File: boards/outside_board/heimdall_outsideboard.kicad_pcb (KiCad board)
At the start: 2 copper layers, 6 parts, among them J1 Conn_01x09, J2 Conn_01x06

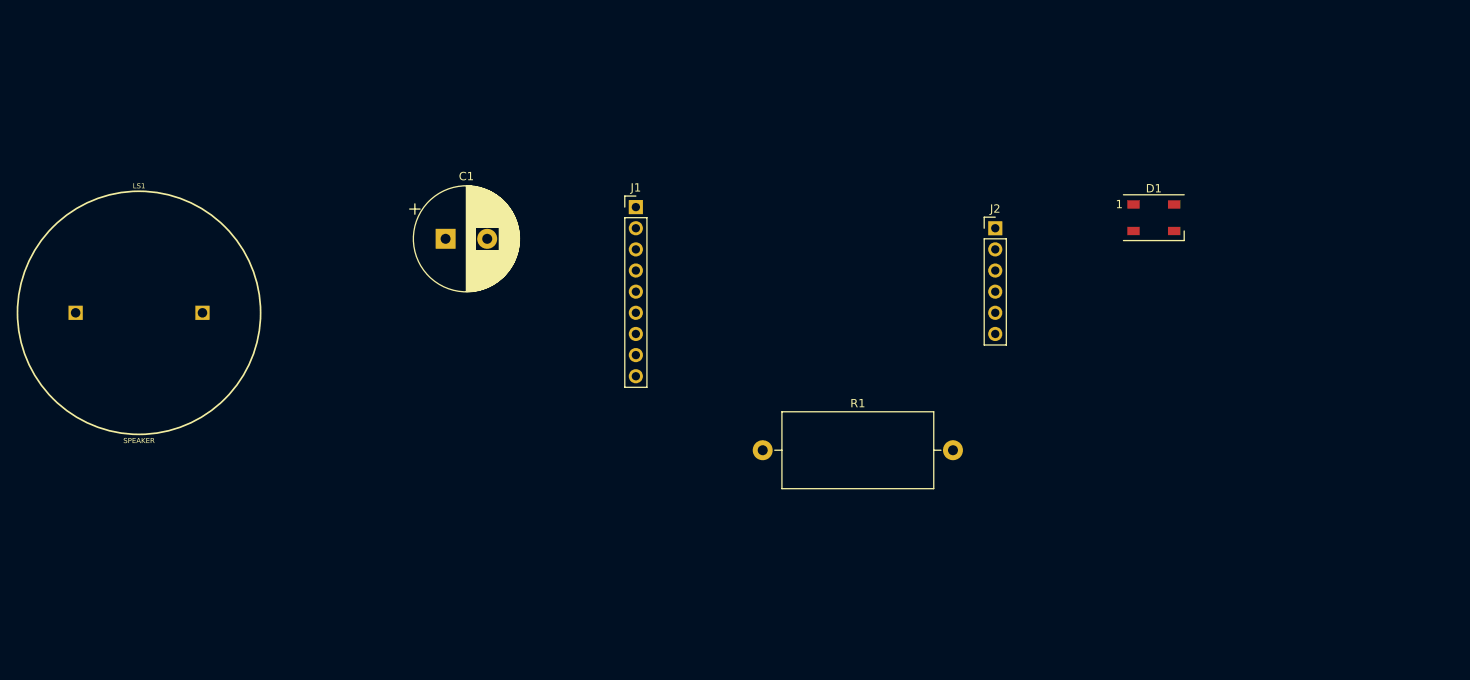
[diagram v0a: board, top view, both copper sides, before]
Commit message: Outside board design: more PCB layout
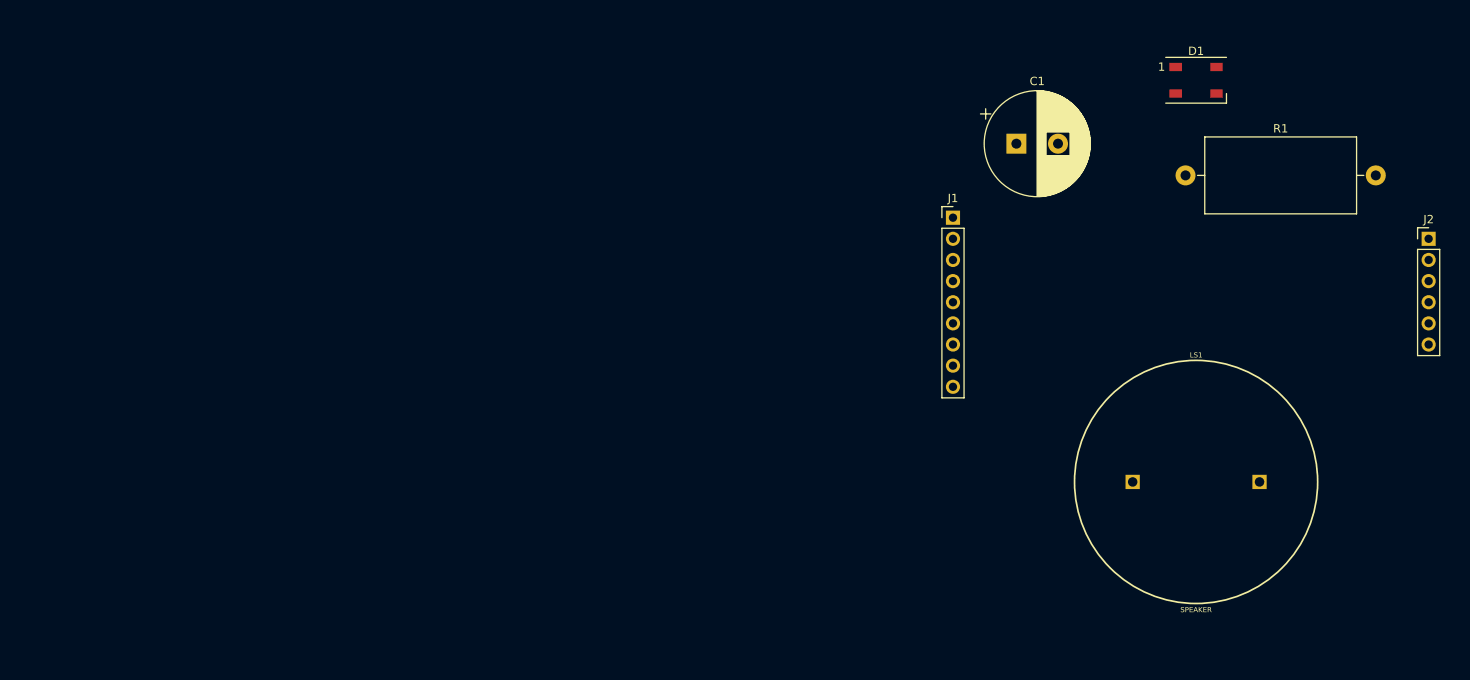
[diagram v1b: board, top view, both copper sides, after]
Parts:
- moved LS1 128.6 mm to (83.8, 130.8)
- moved C1 69.5 mm to (62.2, 90.2)
- moved R1 60.6 mm to (82.5, 94.0)
- moved J2 52.1 mm to (111.8, 101.6)
- moved J1 38.1 mm to (54.6, 99.1)
- moved D1 17.3 mm to (83.8, 82.5)

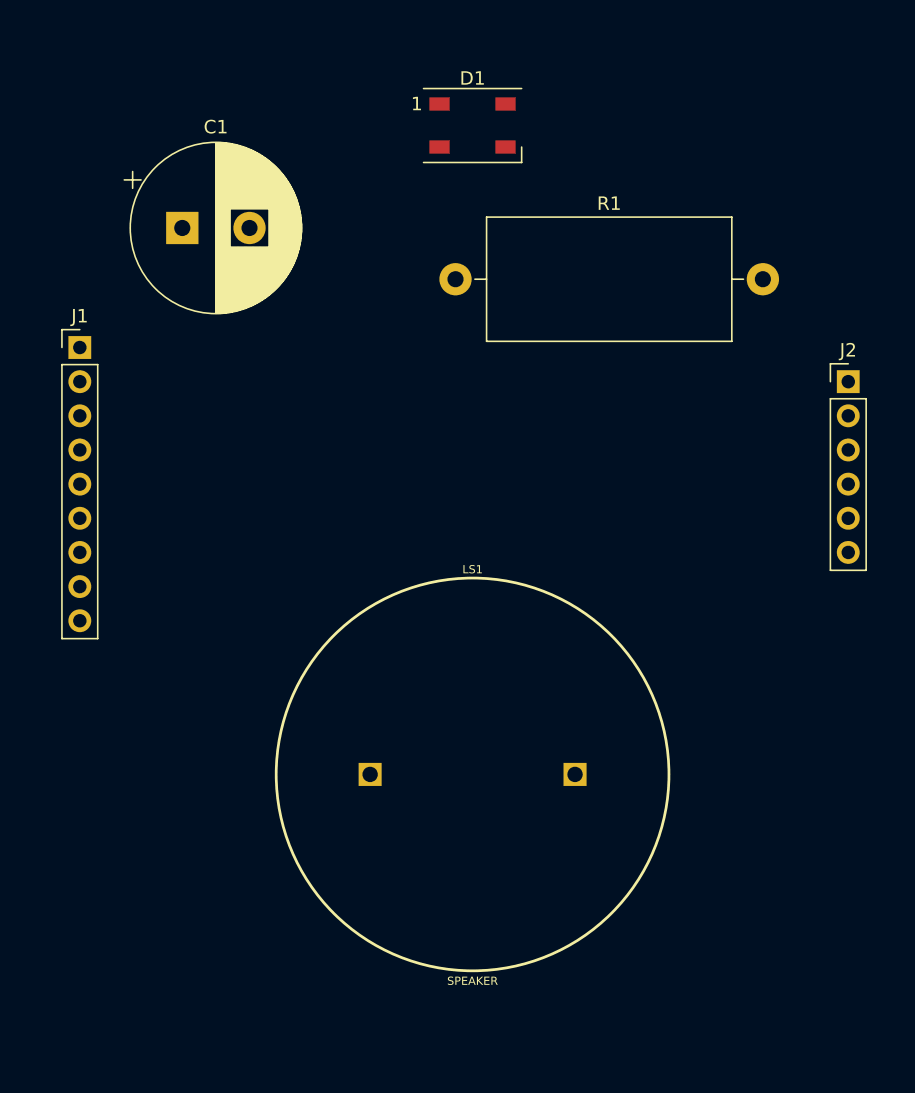
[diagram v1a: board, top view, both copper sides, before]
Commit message: Outside board: replace the pin headers with screw terminals
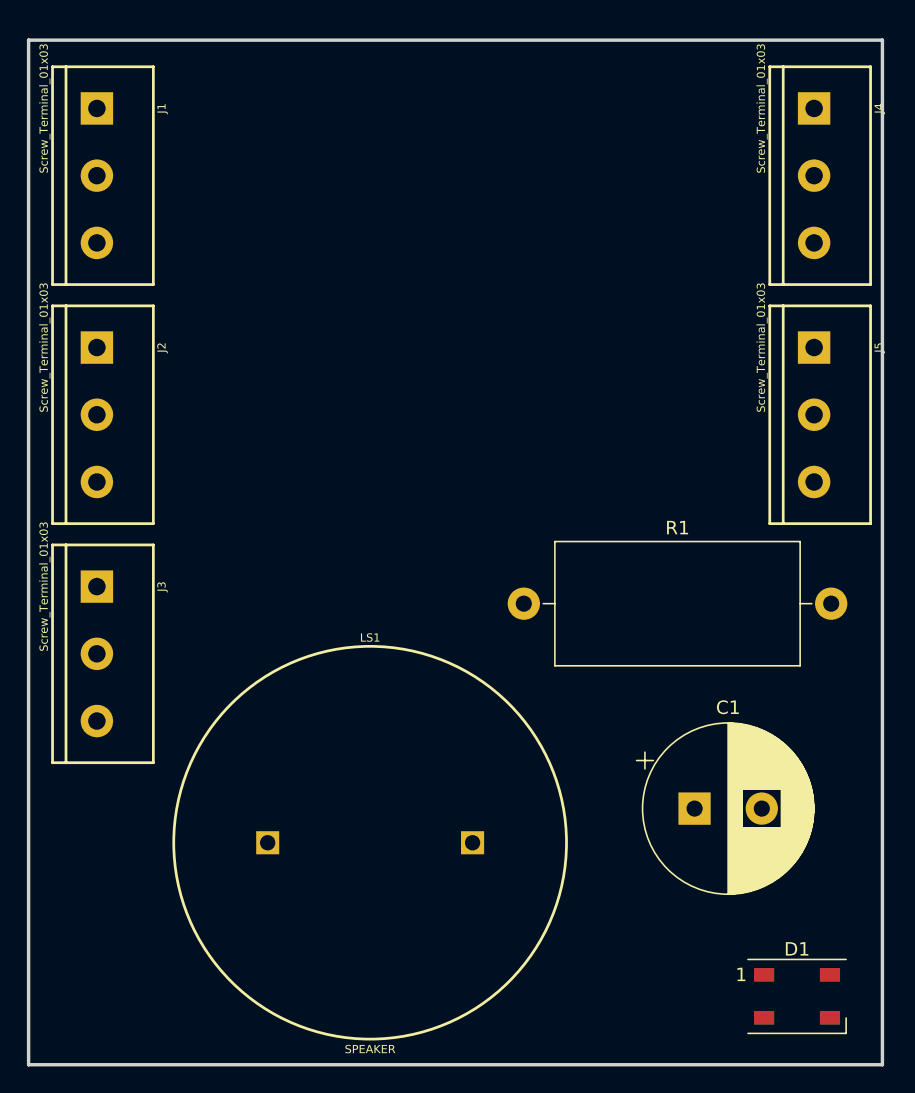
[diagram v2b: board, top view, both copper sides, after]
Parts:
- added J3: Screw_Terminal_01x03, Connectors:SCREWTERMINAL-5MM-3, F.Cu at (55.9, 116.8)
- added J4: Screw_Terminal_01x03, Connectors:SCREWTERMINAL-5MM-3, F.Cu at (109.2, 81.3)
- added J5: Screw_Terminal_01x03, Connectors:SCREWTERMINAL-5MM-3, F.Cu at (109.2, 99.1)
- J1: value Conn_01x09 -> Screw_Terminal_01x03; footprint Connector_PinHeader_2.54mm:PinHeader_1x09_P2.54mm_Vertical -> Connectors:SCREWTERMINAL-5MM-3
- J2: value Conn_01x06 -> Screw_Terminal_01x03; footprint Connector_PinHeader_2.54mm:PinHeader_1x06_P2.54mm_Vertical -> Connectors:SCREWTERMINAL-5MM-3
- moved D1 69.1 mm to (108.0, 147.3)
- moved C1 57.6 mm to (100.3, 133.3)
- moved J2 55.9 mm to (55.9, 99.1), turned to 270 degrees
- moved R1 24.7 mm to (87.6, 118.1)
- moved J1 17.8 mm to (55.9, 81.3), turned to 270 degrees
- moved LS1 9.16 mm to (76.2, 135.9)
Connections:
- J2 pad 1: /+3V3 -> /CS
- J2 pad 2: /GND -> /SCK
- J2 pad 3: /CS -> /MOSI
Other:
- board outline added: 63.5 x 76.2 mm

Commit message: Revert "Outside board: replace the pin headers with screw terminals"
This reverts commit 695c30ad44e01b6420bbd27eb88eba567c36bb63.
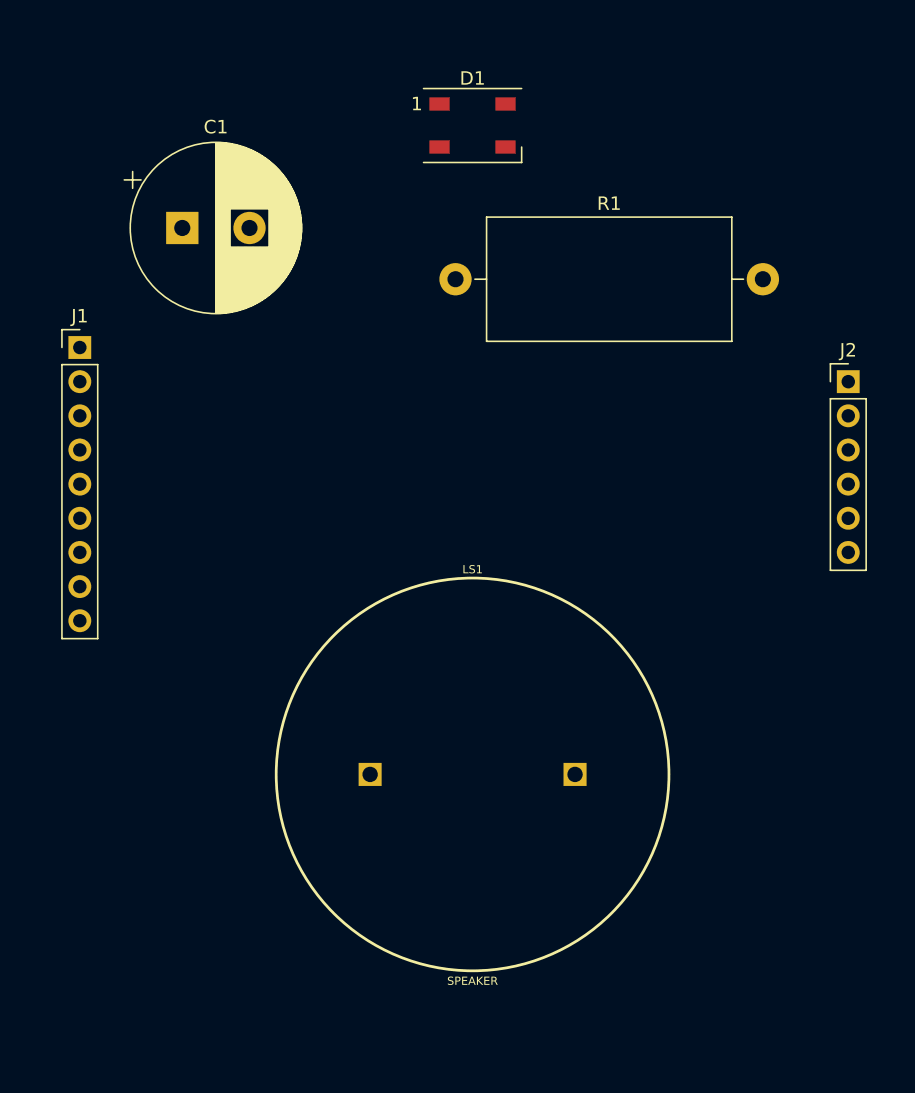
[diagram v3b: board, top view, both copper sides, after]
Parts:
- removed J3, J4, J5: Screw_Terminal_01x03, Connectors:SCREWTERMINAL-5MM-3
- J1: value Screw_Terminal_01x03 -> Conn_01x09; footprint Connectors:SCREWTERMINAL-5MM-3 -> Connector_PinHeader_2.54mm:PinHeader_1x09_P2.54mm_Vertical
- J2: value Screw_Terminal_01x03 -> Conn_01x06; footprint Connectors:SCREWTERMINAL-5MM-3 -> Connector_PinHeader_2.54mm:PinHeader_1x06_P2.54mm_Vertical
- moved D1 69.1 mm to (83.8, 82.5)
- moved C1 57.6 mm to (62.2, 90.2)
- moved J2 55.9 mm to (111.8, 101.6), turned to 0 degrees
- moved R1 24.7 mm to (82.5, 94.0)
- moved J1 17.8 mm to (54.6, 99.1), turned to 0 degrees
- moved LS1 9.16 mm to (83.8, 130.8)
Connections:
- J2 pad 1: /CS -> /+3V3
- J2 pad 2: /SCK -> /GND
- J2 pad 3: /MOSI -> /CS
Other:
- board outline removed

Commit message: More outside board PCB layout.
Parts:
- moved R1 29.8 mm to (59.7, 113.0)
- moved LS1 17.3 mm to (67.3, 135.9)
- moved J2 15.9 mm to (97.8, 94.0)
- moved D1 9.15 mm to (93.0, 82.8)
- moved J1 7.62 mm to (54.6, 91.4)
- moved C1 7.18 mm to (67.3, 85.1)
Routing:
- net Net-(D1-Pad4): track 0.00 -> 51.8 mm
- net /SCK: track 0.00 -> 43.2 mm
- net /MOSI: track 0.00 -> 43.2 mm
- net /MISO: track 0.00 -> 43.2 mm
- net /GND: track 0.00 -> 43.2 mm
- net /CS: track 0.00 -> 43.2 mm
- net /+3V3: track 0.00 -> 43.2 mm
- net /+5V: track 0.00 -> 41.2 mm
- net /Buzzer: track 0.00 -> 27.9 mm
- net /LED: track 0.00 -> 8.00 mm
- added copper zone on B.Cu, net /GND
- added copper zone on F.Cu, net /GND
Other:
- board outline added: 50.8 x 76.2 mm
- board text added: "Heimdall Access Control Board"
- board text added: "github.com/makesaltlake/heimdall"

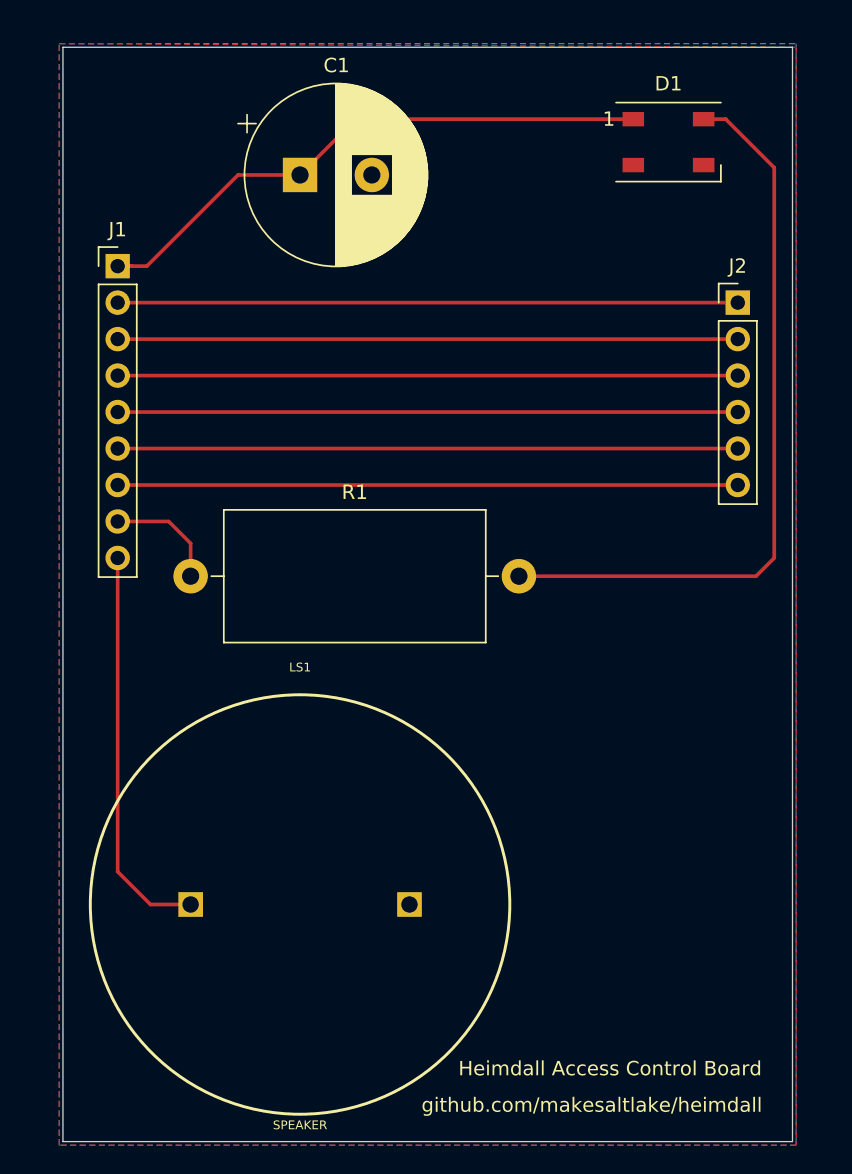
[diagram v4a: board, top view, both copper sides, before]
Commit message: Update outside board schematics and board layout
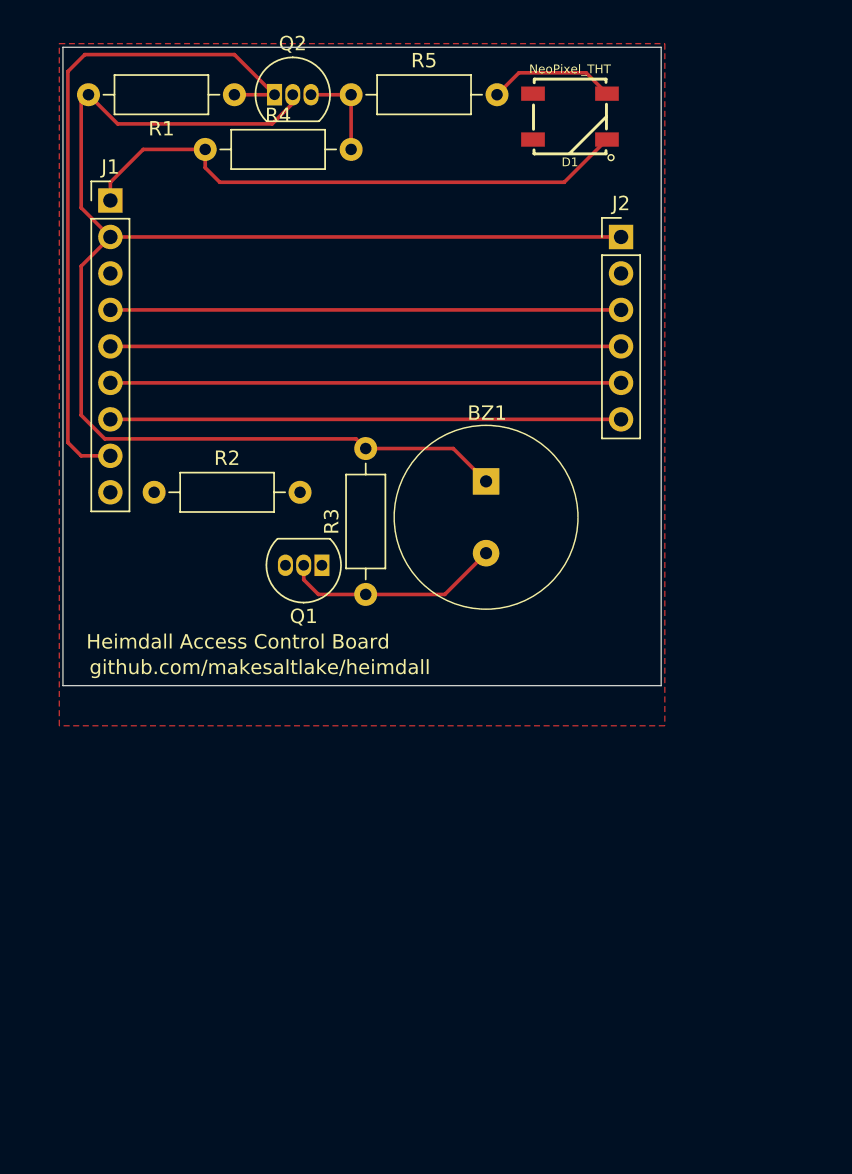
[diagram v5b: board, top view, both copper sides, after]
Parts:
- removed C1: 1000UF-RADIAL-5MM-25V-20%, Capacitor_THT:CP_Radial_D12.5mm_P5.00mm
- removed LS1: SPEAKER, Electromechanical:PCB_MOUNT_SPEAKER
- added BZ1: PS1240P02BT, digikey-footprints:Piezo_Transducer_THT_PS1240P02BT, F.Cu at (80.3, 106.4)
- added Q1: 2N3904, Package_TO_SOT_THT:TO-92_Inline, F.Cu at (68.8, 112.3)
- added Q2: 2N7000, Package_TO_SOT_THT:TO-92_Inline, F.Cu at (65.5, 79.5)
- added R2: 1K, Resistor_THT:R_Axial_DIN0207_L6.3mm_D2.5mm_P10.16mm_Horizontal, F.Cu at (57.1, 107.2)
- added R3: 1K, Resistor_THT:R_Axial_DIN0207_L6.3mm_D2.5mm_P10.16mm_Horizontal, F.Cu at (71.9, 114.3)
- added R4: 10K, Resistor_THT:R_Axial_DIN0207_L6.3mm_D2.5mm_P10.16mm_Horizontal, F.Cu at (60.7, 83.3)
- added R5: 470, Resistor_THT:R_Axial_DIN0207_L6.3mm_D2.5mm_P10.16mm_Horizontal, F.Cu at (70.9, 79.5)
- D1: value WS2812B -> NeoPixel_THT; footprint LED_SMD:LED_WS2812B_PLCC4_5.0x5.0mm_P3.2mm -> LED:WS2812B
- R1: value 470OHM -> 10K; footprint Resistor_THT:R_Axial_DIN0918_L18.0mm_D9.0mm_P22.86mm_Horizontal -> Resistor_THT:R_Axial_DIN0207_L6.3mm_D2.5mm_P10.16mm_Horizontal
- moved R1 33.7 mm to (62.7, 79.5), turned to 180 degrees
- moved J2 9.33 mm to (89.7, 89.4)
- moved D1 7.08 mm to (86.1, 81.0), turned to 180 degrees
- moved J1 4.60 mm to (54.1, 86.9)
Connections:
- D1 pad 1: /+5V -> Net-(D1-Pad1)
- D1 pad 2: Net-(D1-Pad2) -> GND
- D1 pad 3: /GND -> +5V
- J1 pad 1: /+5V -> +5V
- J1 pad 2: /+3V3 -> +3V3
- J1 pad 3: /GND -> GND
- J2 pad 1: /+3V3 -> +3V3
- J2 pad 2: /GND -> GND
- R1 pad 2: Net-(D1-Pad4) -> +3V3
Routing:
- net +3V3: track 0.00 -> 106.1 mm
- net /GND: track 43.2 -> 0.00 mm
- net /+3V3: track 43.2 -> 0.00 mm
- net Net-(D1-Pad4): track 51.8 -> 8.89 mm
- net /+5V: track 41.2 -> 0.00 mm
- net /LED: track 8.00 -> 48.0 mm
- net +5V: track 0.00 -> 39.7 mm
- net /Buzzer: track 27.9 -> 0.00 mm
- net Net-(BZ1-Pad2): track 0.00 -> 15.3 mm
- net /SCK: track 43.2 -> 35.6 mm
- net /MOSI: track 43.2 -> 35.6 mm
- net /MISO: track 43.2 -> 35.6 mm
- net /CS: track 43.2 -> 35.6 mm
- net Net-(Q2-Pad3): track 0.00 -> 6.60 mm
- added copper zone on F.Cu, net GND
- removed copper zone on B.Cu, net /GND
- removed copper zone on F.Cu, net /GND
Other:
- board size 50.8 x 76.2 mm -> 41.7 x 44.5 mm
- net class Default: clearance 0.254 -> 0.2032
- rule pad_to_mask_clearance: 0.0508 -> 0
- rule trace_clearance: 0.254 -> 0.2032
